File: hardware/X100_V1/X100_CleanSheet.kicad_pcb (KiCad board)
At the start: 4 copper layers, 45 x 45 mm, 205 parts, among them J401 124019772112A, J501 1040310811, J601 SM04B-GHS-TB(LF)(SN), J701 SM06B-GHS-TB(LF)(SN), J702 SM06B-GHS-TB(LF)(SN), J703 SM06B-GHS-TB(LF)(SN), J704 SM04B-GHS-TB(LF)(SN), J801 OUT1 /GND, J802 OUT2 /GND, J803 OUT3 /GND, J804 OUT4 /GND, J805 OUT5 /GND, J806 OUT6 /GND, J807 SWD:1REF2GND3IO4CLK5NRST, J808 BATTERY/bench3S-6S ONLY, J809 CURRENT monitor only, Q101 DMP6023LSS-13, U101 TPS54360BDDAR, U102 AP63203WU-7, U103 TPS7A2033PDBVR, U104 TPS2553DBVR, U201 STM32H743VIT6, U301 BMI088, U302 SPL06-001, U401 TPD2E2U06QDBZRQ1, U402 SN74LVC1G17DBVR, U403 TPD2E2U06QDBZRQ1, U404 TPD2E2U06QDBZRQ1, U601 TCAN3414DR, U801 TMUX1511PWR, Y201 8.000MHz /CL20pF

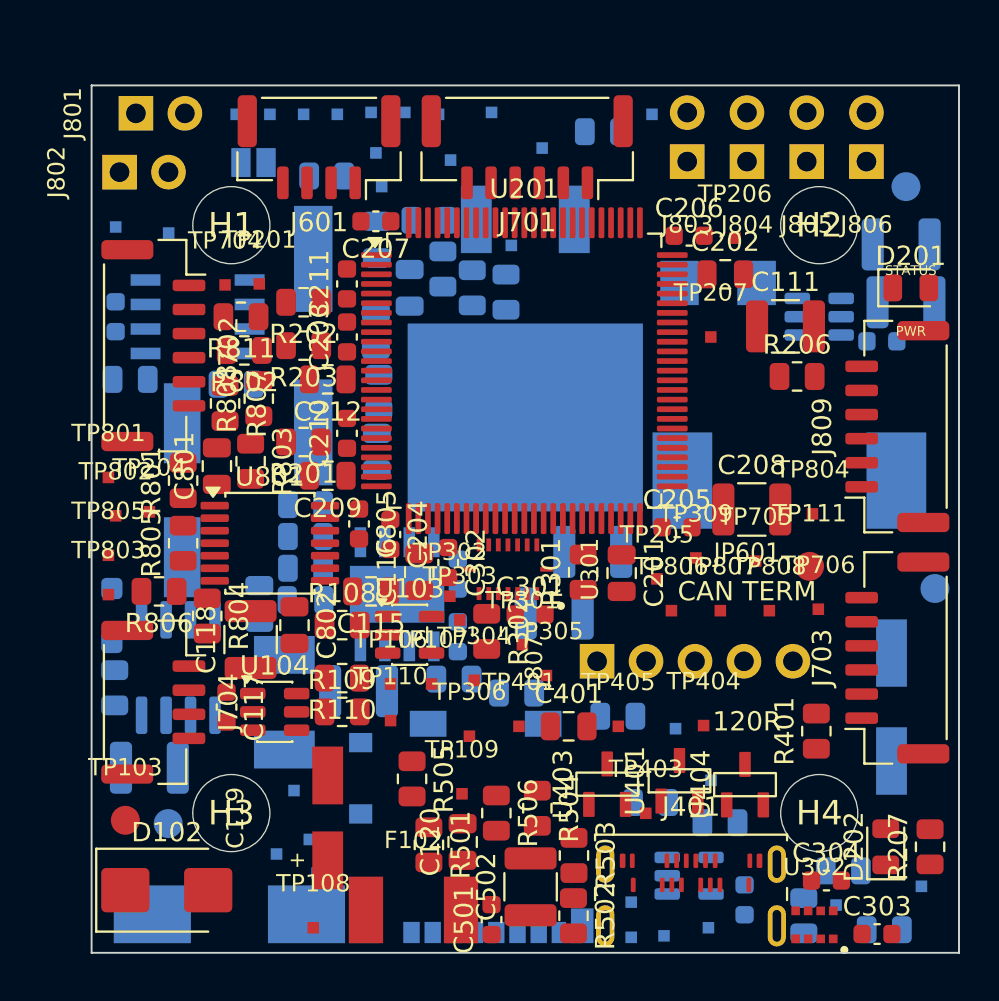
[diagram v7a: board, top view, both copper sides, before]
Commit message: 整体平移MCU局部去耦释放ADC侧布局空间
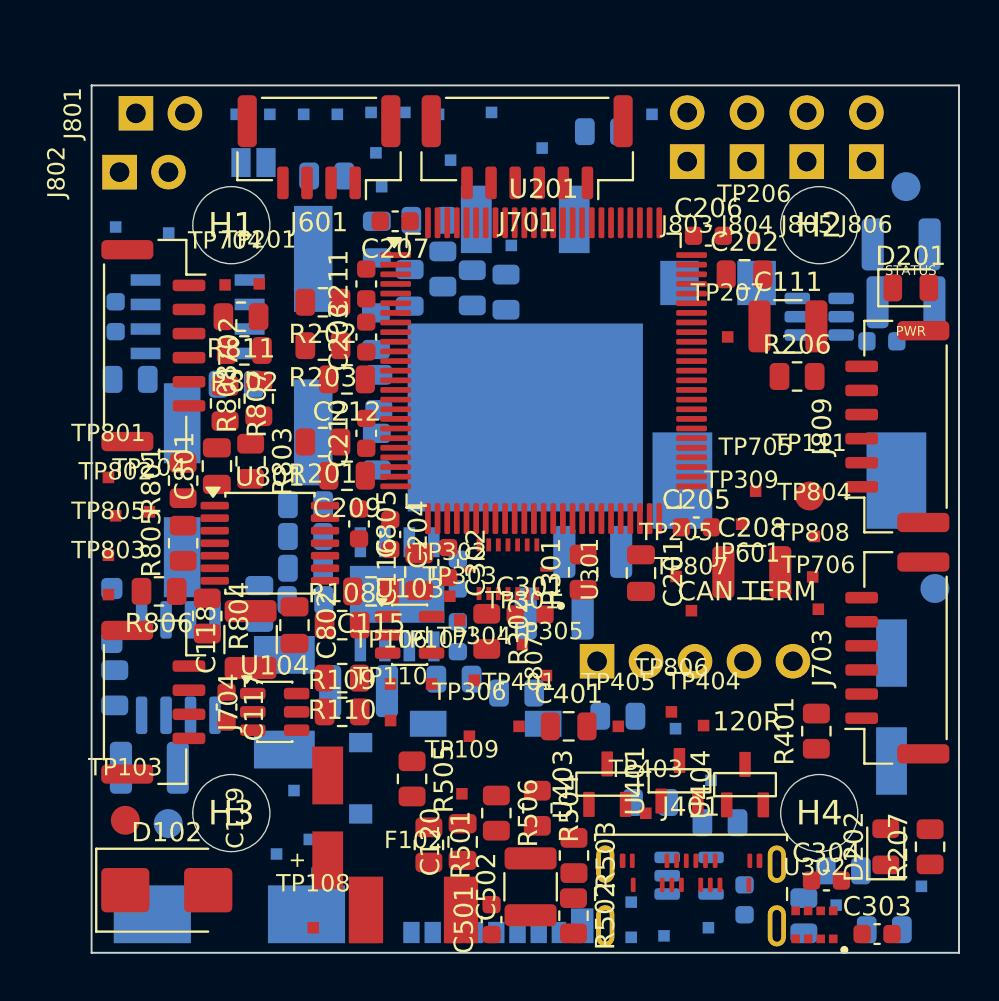
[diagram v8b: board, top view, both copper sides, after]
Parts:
- moved TP806 5.25 mm to (107.6, 110.0)
- moved TP111 3.65 mm to (114.8, 98.8)
- moved TP705 3.62 mm to (112.0, 98.5)
- moved C208 3.25 mm to (111.8, 102.8)
- moved TP309 2.95 mm to (111.2, 100.3)
- moved TP808 2.85 mm to (114.9, 103.0)
- moved TP807 1.50 mm to (108.6, 104.8)
- moved TP804 1.18 mm to (115.0, 100.9)
- moved TP205 1.01 mm to (107.8, 103.0)
- moved C201 1.00 mm to (106.0, 102.8)
- moved C202 1.00 mm to (111.4, 87.3)
- moved C203 1.00 mm to (91.8, 90.5)
- moved C205 1.00 mm to (108.9, 100.4)
- moved C206 1.00 mm to (109.5, 85.3)
- moved C207 1.00 mm to (93.2, 84.5)
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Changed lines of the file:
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@@
 	(footprint "X100_Physical:Official_Capacitor_SMD_C_0603_1608Metric"
 		(layer "F.Cu")
-		(at 90.75 87.8 90)
+		(at 91.75 87.8 90)
 		(descr "Capacitor SMD 0603 (1608 Metric), square (rectangular) end terminal, IPC-7351 nominal, (Body size source: IPC-SM-782 page 76, https://www.pcb-3d.com/wordpress/wp-content/uploads/ipc-sm-782a_amendment_1_and_2.pdf)")
 		(tags "capacitor")
@@
 	(footprint "X100_Physical:Official_Resistor_SMD_R_0805_2012Metric"
 		(layer "F.Cu")
-		(at 88.5 96 180)
+		(at 89.5 96 180)
 		(descr "Resistor SMD 0805 (2012 Metric), square (rectangular) end terminal, IPC-7351 nominal, (Body size source: IPC-SM-782 page 72, https://www.pcb-3d.com/wordpress/wp-content/uploads/ipc-sm-782a_amendment_1_and_2.pdf)")
 		(tags "resistor")
@@
 	(footprint "X100_Physical:Official_Capacitor_SMD_C_1210_3225Metric"
 		(layer "F.Cu")
-		(at 113.5 90)
+		(at 113.625 90)
 		(descr "Capacitor SMD 1210 (3225 Metric), square (rectangular) end terminal, IPC-7351 nominal, (Body size source: IPC-SM-782 page 76, https://www.pcb-3d.com/wordpress/wp-content/uploads/ipc-sm-782a_amendment_1_and_2.pdf)")
 		(tags "capacitor")
@@
 	(footprint "X100_Physical:TP0p6_Inline_NoPaste"
 		(layer "F.Cu")
-		(at 109.625 90.55)
+		(at 110.5 90.55)
 		(descr "Project0.6mm inline probe pad; high speed no long branch; no hole; no paste")
 		(property "Reference" "TP207"
@@
 	(footprint "X100_Physical:Official_Capacitor_SMD_C_0603_1608Metric"
 		(layer "F.Cu")
-		(at 108.5 85.3)
+		(at 109.5 85.3)
 		(descr "Capacitor SMD 0603 (1608 Metric), square (rectangular) end terminal, IPC-7351 nominal, (Body size source: IPC-SM-782 page 76, https://www.pcb-3d.com/wordpress/wp-content/uploads/ipc-sm-782a_amendment_1_and_2.pdf)")
 		(tags "capacitor")
@@
 	(footprint "X100_Physical:TP0p6_Inline_NoPaste"
 		(layer "F.Cu")
-		(at 108.85 102.013)
+		(at 111.225 100.263)
 		(descr "Project0.6mm inline probe pad; high speed no long branch; no hole; no paste")
 		(property "Reference" "TP309"
@@
 	(footprint "X100_Physical:TP0p6_Inline_NoPaste"
 		(layer "F.Cu")
-		(at 110.875 85.425)
+		(at 111.875 85.425)
 		(descr "Project0.6mm inline probe pad; high speed no long branch; no hole; no paste")
 		(property "Reference" "TP206"
@@
 	(footprint "X100_Physical:Official_Capacitor_SMD_C_0603_1608Metric"
 		(layer "F.Cu")
-		(at 107.875 100.425)
+		(at 108.875 100.425)
 		(descr "Capacitor SMD 0603 (1608 Metric), square (rectangular) end terminal, IPC-7351 nominal, (Body size source: IPC-SM-782 page 76, https://www.pcb-3d.com/wordpress/wp-content/uploads/ipc-sm-782a_amendment_1_and_2.pdf)")
 		(tags "capacitor")
@@
 	(footprint "X100_Physical:TP0p6_Inline_NoPaste"
 		(layer "F.Cu")
-		(at 110.12 104.75)
+		(at 108.62 104.75)
 		(descr "Project0.6mm inline probe pad; high speed no long branch; no hole; no paste")
 		(property "Reference" "TP807"
@@
 	(footprint "X100_Physical:Official_Capacitor_SMD_C_0603_1608Metric"
 		(layer "F.Cu")
-		(at 90.75 95.55 90)
+		(at 91.75 95.55 90)
 		(descr "Capacitor SMD 0603 (1608 Metric), square (rectangular) end terminal, IPC-7351 nominal, (Body size source: IPC-SM-782 page 76, https://www.pcb-3d.com/wordpress/wp-content/uploads/ipc-sm-782a_amendment_1_and_2.pdf)")
 		(tags "capacitor")
@@
 	(footprint "X100_Physical:Official_Resistor_SMD_R_0805_2012Metric"
 		(layer "F.Cu")
-		(at 88.5 91 180)
+		(at 89.5 91 180)
 		(descr "Resistor SMD 0805 (2012 Metric), square (rectangular) end terminal, IPC-7351 nominal, (Body size source: IPC-SM-782 page 72, https://www.pcb-3d.com/wordpress/wp-content/uploads/ipc-sm-782a_amendment_1_and_2.pdf)")
 		(tags "resistor")
@@
 	(footprint "X100_Physical:TP0p6_Inline_NoPaste"
 		(layer "F.Cu")
-		(at 106.825 103.1)
+		(at 107.825 102.975)
 		(descr "Project0.6mm inline probe pad; high speed no long branch; no hole; no paste")
 		(property "Reference" "TP205"
@@
 	(footprint "X100_Physical:Official_Capacitor_SMD_C_0603_1608Metric"
 		(layer "F.Cu")
-		(at 92.25 84.55 180)
+		(at 93.25 84.55 180)
 		(descr "Capacitor SMD 0603 (1608 Metric), square (rectangular) end terminal, IPC-7351 nominal, (Body size source: IPC-SM-782 page 76, https://www.pcb-3d.com/wordpress/wp-content/uploads/ipc-sm-782a_amendment_1_and_2.pdf)")
 		(tags "capacitor")
@@
 	(footprint "X100_Physical:Official_Capacitor_SMD_C_0805_2012Metric"
 		(layer "F.Cu")
-		(at 105 102.8 -90)
+		(at 106 102.8 -90)
 		(descr "Capacitor SMD 0805 (2012 Metric), square (rectangular) end terminal, IPC-7351 nominal, (Body size source: IPC-SM-782 page 76, https://www.pcb-3d.com/wordpress/wp-content/uploads/ipc-sm-782a_amendment_1_and_2.pdf, https://docs.google.com/spreadsheets/d/1BsfQQcO9C6DZCsRaXUlFlo91Tg2WpOkGARC1WS5S8t0/edit?usp=sharing)")
 		(tags "capacitor")
@@
 	(footprint "X100_Physical:Official_Capacitor_SMD_C_0805_2012Metric"
 		(layer "F.Cu")
-		(at 89.75 97.75 180)
+		(at 90.75 97.75 180)
 		(descr "Capacitor SMD 0805 (2012 Metric), square (rectangular) end terminal, IPC-7351 nominal, (Body size source: IPC-SM-782 page 76, https://www.pcb-3d.com/wordpress/wp-content/uploads/ipc-sm-782a_amendment_1_and_2.pdf, https://docs.google.com/spreadsheets/d/1BsfQQcO9C6DZCsRaXUlFlo91Tg2WpOkGARC1WS5S8t0/edit?usp=sharing)")
 		(tags "capacitor")
@@
 	(footprint "X100_Physical:Official_Capacitor_SMD_C_0603_1608Metric"
 		(layer "F.Cu")
-		(at 90.75 90.55 90)
+		(at 91.75 90.55 90)
 		(descr "Capacitor SMD 0603 (1608 Metric), square (rectangular) end terminal, IPC-7351 nominal, (Body size source: IPC-SM-782 page 76, https://www.pcb-3d.com/wordpress/wp-content/uploads/ipc-sm-782a_amendment_1_and_2.pdf)")
 		(tags "capacitor")
@@
 	(footprint "X100_Physical:Official_Resistor_SMD_R_0805_2012Metric"
 		(layer "F.Cu")
-		(at 88.5 88.75 180)
+		(at 89.5 88.75 180)
 		(descr "Resistor SMD 0805 (2012 Metric), square (rectangular) end terminal, IPC-7351 nominal, (Body size source: IPC-SM-782 page 72, https://www.pcb-3d.com/wordpress/wp-content/uploads/ipc-sm-782a_amendment_1_and_2.pdf)")
 		(tags "resistor")
@@
 	(footprint "X100_Physical:Official_Package_QFP_LQFP-100_14x14mm_P0.5mm"
 		(layer "F.Cu")
-		(at 99.95 92.3)
+		(at 100.95 92.3)
 		(descr "LQFP, 100 Pin (https://www.nxp.com/docs/en/package-information/SOT407-1.pdf)")
 		(tags "LQFP QFP")
@@
 	(footprint "X100_Physical:Official_Capacitor_SMD_C_0805_2012Metric"
 		(layer "F.Cu")
-		(at 110.375 87.3)
+		(at 111.375 87.3)
 		(descr "Capacitor SMD 0805 (2012 Metric), square (rectangular) end terminal, IPC-7351 nominal, (Body size source: IPC-SM-782 page 76, https://www.pcb-3d.com/wordpress/wp-content/uploads/ipc-sm-782a_amendment_1_and_2.pdf, https://docs.google.com/spreadsheets/d/1BsfQQcO9C6DZCsRaXUlFlo91Tg2WpOkGARC1WS5S8t0/edit?usp=sharing)")
 		(tags "capacitor")
@@
 	(footprint "X100_Physical:Official_Capacitor_SMD_C_0805_2012Metric"
 		(layer "F.Cu")
-		(at 89.75 92.75 180)
+		(at 90.75 92.75 180)
 		(descr "Capacitor SMD 0805 (2012 Metric), square (rectangular) end terminal, IPC-7351 nominal, (Body size source: IPC-SM-782 page 76, https://www.pcb-3d.com/wordpress/wp-content/uploads/ipc-sm-782a_amendment_1_and_2.pdf, https://docs.google.com/spreadsheets/d/1BsfQQcO9C6DZCsRaXUlFlo91Tg2WpOkGARC1WS5S8t0/edit?usp=sharing)")
 		(tags "capacitor")
@@
 	(footprint "X100_Physical:TP0p6_Inline_NoPaste"
 		(layer "F.Cu")
-		(at 114.9 99.725)
+		(at 115 100.9)
 		(descr "Project0.6mm inline probe pad; high speed no long branch; no hole; no paste")
 		(property "Reference" "TP804"
@@
 	(footprint "X100_Physical:Official_Capacitor_SMD_C_1210_3225Metric"
 		(layer "F.Cu")
-		(at 111.75 99.5)
+		(at 111.75 102.75)
 		(descr "Capacitor SMD 1210 (3225 Metric), square (rectangular) end terminal, IPC-7351 nominal, (Body size source: IPC-SM-782 page 76, https://www.pcb-3d.com/wordpress/wp-content/uploads/ipc-sm-782a_amendment_1_and_2.pdf)")
 		(tags "capacitor")
@@
 	(footprint "X100_Physical:TP0p6_Inline_NoPaste"
 		(layer "F.Cu")
-		(at 112.66 104.75)
+		(at 114.91 103)
 		(descr "Project0.6mm inline probe pad; high speed no long branch; no hole; no paste")
 		(property "Reference" "TP808"
@@
 	(footprint "X100_Physical:TP0p6_Inline_NoPaste"
 		(layer "F.Cu")
-		(at 107.58 104.75)
+		(at 107.58 110)
 		(descr "Project0.6mm inline probe pad; high speed no long branch; no hole; no paste")
 		(property "Reference" "TP806"
@@
 	(footprint "X100_Physical:TP0p6_Inline_NoPaste"
 		(layer "F.Cu")
-		(at 111.95 102.175)
+		(at 111.95 98.55)
 		(descr "Project0.6mm inline probe pad; high speed no long branch; no hole; no paste")
 		(property "Reference" "TP705"
@@
 	(footprint "X100_Physical:TP1p5_NoPaste"
 		(layer "F.Cu")
-		(at 114.75 102.45)
+		(at 114.75 98.8)
 		(descr "Project1.5mm round accessible top test pad; no hole; no paste")
 		(property "Reference" "TP111"
